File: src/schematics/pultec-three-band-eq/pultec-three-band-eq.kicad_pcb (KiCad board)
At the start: 2 copper layers, 55 parts, among them J1 IN, J10 Low Boost Select Return, J11 Low Boost Level, J12 Hi Cut Select Return, J13 Frequency Selector Send, J19 Inductor Return, J2 OUT, J20 Boost High Q, J21 Boost High, J22 100mH, J23 200mH, J24 300mH, J25 600mH, J3 Hi Cut Select Send, J4 HI CUT, J5 Low Cut Select Send, J6 Low Boost Select Send, J7 Low Cut Level, J8 High Boost Selector Return, J9 Low Cut Select Return

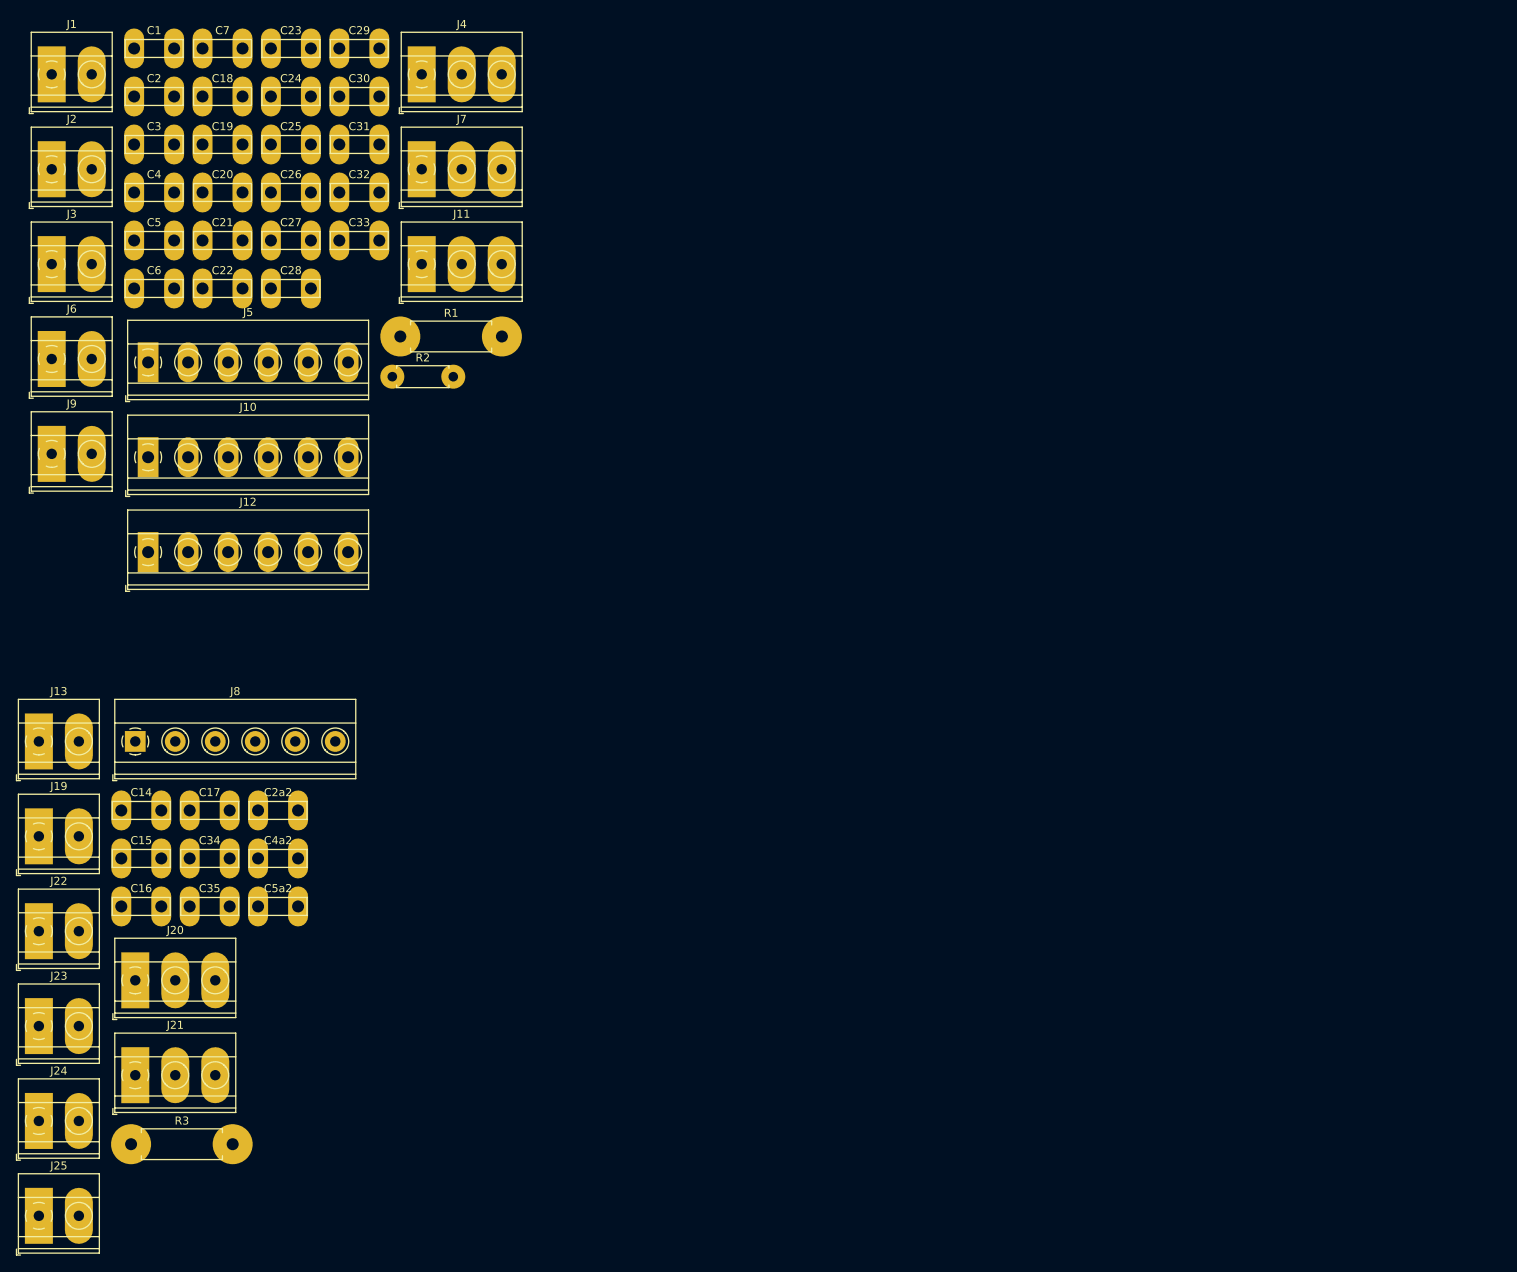
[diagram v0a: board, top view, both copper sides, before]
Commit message: - fixed unrouted traces
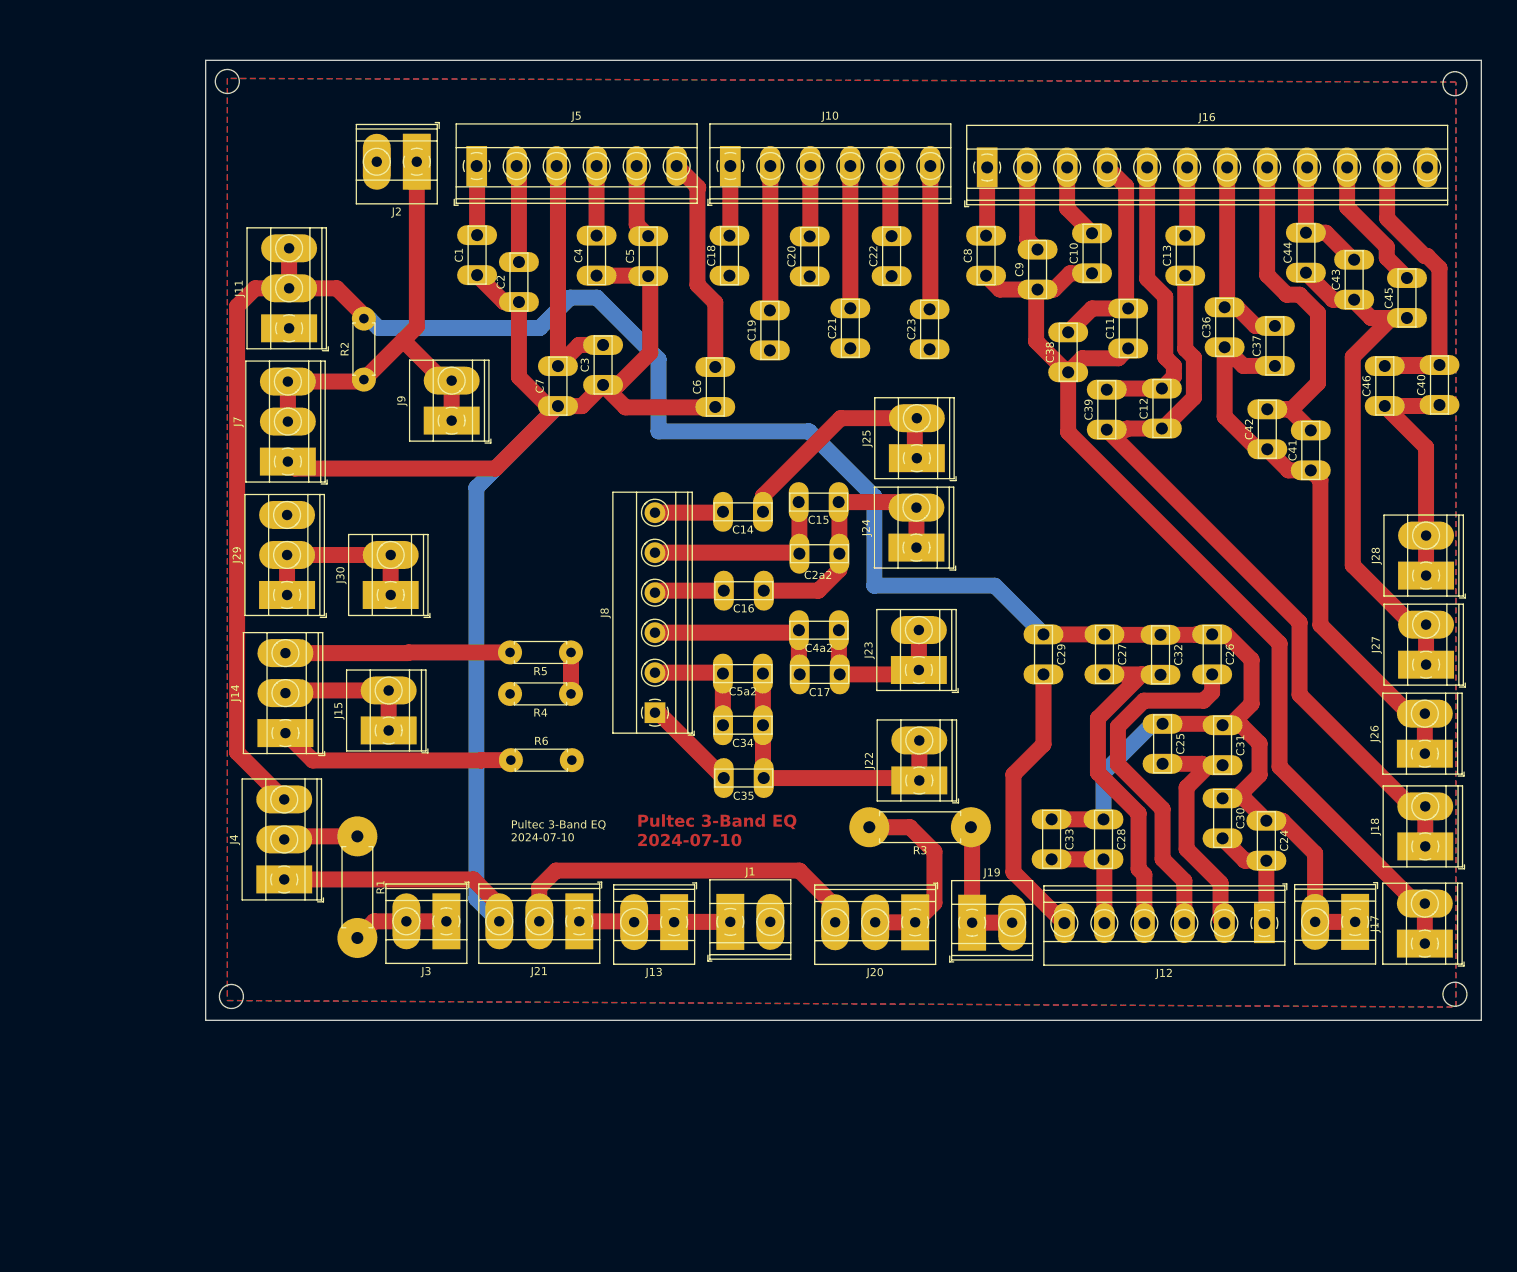
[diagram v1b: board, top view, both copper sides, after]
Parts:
- added C10: 47n, OL Library:C_Rect_L7.0mm_W2.0mm_P5.00mm_Fat_Pad, F.Cu at (151.2, 47.3)
- added C11: 22n, OL Library:C_Rect_L7.0mm_W2.0mm_P5.00mm_Fat_Pad, F.Cu at (155.8, 56.7)
- added C12: 22n, OL Library:C_Rect_L7.0mm_W2.0mm_P5.00mm_Fat_Pad, F.Cu at (160.0, 66.8)
- added C13: 12n, OL Library:C_Rect_L7.0mm_W2.0mm_P5.00mm_Fat_Pad, F.Cu at (162.9, 47.6)
- added C36: 12n, OL Library:C_Rect_L7.0mm_W2.0mm_P5.00mm_Fat_Pad, F.Cu at (167.8, 56.6)
- added C37: 2n2, OL Library:C_Rect_L7.0mm_W2.0mm_P5.00mm_Fat_Pad, F.Cu at (174.1, 58.9)
- added C38: 3n3, OL Library:C_Rect_L7.0mm_W2.0mm_P5.00mm_Fat_Pad, F.Cu at (148.3, 59.7)
- added C39: 3n3, OL Library:C_Rect_L7.0mm_W2.0mm_P5.00mm_Fat_Pad, F.Cu at (153.1, 66.9)
- added C40: 1n, OL Library:C_Rect_L7.0mm_W2.0mm_P5.00mm_Fat_Pad, F.Cu at (194.7, 63.8)
- added C41: 4n7, OL Library:C_Rect_L7.0mm_W2.0mm_P5.00mm_Fat_Pad, F.Cu at (178.6, 72.0)
- added C42: 1n5, OL Library:C_Rect_L7.0mm_W2.0mm_P5.00mm_Fat_Pad, F.Cu at (173.1, 69.3)
- added C43: 4n7, OL Library:C_Rect_L7.0mm_W2.0mm_P5.00mm_Fat_Pad, F.Cu at (184.0, 50.6)
- added C44: 2n2, OL Library:C_Rect_L7.0mm_W2.0mm_P5.00mm_Fat_Pad, F.Cu at (178.0, 47.3)
- added C45: 4n7, OL Library:C_Rect_L7.0mm_W2.0mm_P5.00mm_Fat_Pad, F.Cu at (190.6, 52.9)
- added C46: 2n2, OL Library:C_Rect_L7.0mm_W2.0mm_P5.00mm_Fat_Pad, F.Cu at (187.8, 63.9)
- added C8: 33n, OL Library:C_Rect_L7.0mm_W2.0mm_P5.00mm_Fat_Pad, F.Cu at (138.0, 47.7)
- added C9: 150n, OL Library:C_Rect_L7.0mm_W2.0mm_P5.00mm_Fat_Pad, F.Cu at (144.4, 49.4)
- added J14: Mid bst/cut switch, OL Library:TerminalBlock_Phoenix_MKDS-1,5-3_1x03_P5.00mm_Horizontal Fat Pad, F.Cu at (50.4, 104.8)
- added J15: Mid Sel Ret, OL Library:TerminalBlock_Phoenix_MKDS-1,5-2_1x02_P5.00mm_Horizontal Fat Pad, F.Cu at (63.3, 104.5)
- added J16: Mid Sel Ret, OL Library:TerminalBlock_Phoenix_MKDS-1,5-12_1x12_P5.00mm_Horizontal_Fat_Pad, F.Cu at (138.1, 34.1)
- added J17: 2H, OL Library:TerminalBlock_Phoenix_MKDS-1,5-2_1x02_P5.00mm_Horizontal Fat Pad, F.Cu at (192.8, 131.1)
- added J18: 1H, OL Library:TerminalBlock_Phoenix_MKDS-1,5-2_1x02_P5.00mm_Horizontal Fat Pad, F.Cu at (192.9, 119.0)
- added J26: .45H, OL Library:TerminalBlock_Phoenix_MKDS-1,5-2_1x02_P5.00mm_Horizontal Fat Pad, F.Cu at (192.8, 107.4)
- added J27: .22H, OL Library:TerminalBlock_Phoenix_MKDS-1,5-2_1x02_P5.00mm_Horizontal Fat Pad, F.Cu at (193.0, 96.3)
- added J28: .1H, OL Library:TerminalBlock_Phoenix_MKDS-1,5-2_1x02_P5.00mm_Horizontal Fat Pad, F.Cu at (193.0, 85.1)
- added J29: Mid Lvl (47 Log), OL Library:TerminalBlock_Phoenix_MKDS-1,5-3_1x03_P5.00mm_Horizontal Fat Pad, F.Cu at (50.6, 87.6)
- added J30: Mid Sel Snd, OL Library:TerminalBlock_Phoenix_MKDS-1,5-2_1x02_P5.00mm_Horizontal Fat Pad, F.Cu at (63.6, 87.6)
- added R4: 100K, OL Library:R_Axial_DIN0207_L6.3mm_D2.5mm_P7.62mm_Horizontal, F.Cu at (86.1, 99.9)
- added R5: 4K7, OL Library:R_Axial_DIN0207_L6.3mm_D2.5mm_P7.62mm_Horizontal, F.Cu at (86.1, 94.7)
- added R6: 1K, OL Library:R_Axial_DIN0207_L6.3mm_D2.5mm_P7.62mm_Horizontal, F.Cu at (78.6, 108.2)
- J10: value Low Boost Select Return -> Lo Boost Sel Ret
- J11: value Low Boost Level -> Lo Boost Lvl
- J12: value Hi Cut Select Return -> Hi Cut Sel Ret
- J13: value Frequency Selector Send -> Hi Boost Sel Snd
- J19: value Inductor Return -> Hi Boost Sel Ret
- J20: value Boost High Q -> Hi Boost Q
- J21: value Boost High -> Hi Boost Lvl
- J3: value Hi Cut Select Send -> Hi Cut Sel Snd
- J4: value HI CUT -> Hi Cut Lvl
- J5: value Low Cut Select Send -> Lo Cut Sel Snd
- J6: value Low Boost Select Send -> Lo Boost Sel Snd
- J7: value Low Cut Level -> Low Cut Lvl
- J8: value High Boost Selector Return -> Hi Boost Sel Rtn
- J9: value Low Cut Select Return -> Low Cut Sel Ret
- moved J6 177.5 mm to (184.1, 128.4), turned to 180 degrees
- moved C24 153.9 mm to (173.0, 115.8), turned to -90 degrees
- moved J12 147.0 mm to (172.8, 128.6), turned to 180 degrees
- moved J25 145.0 mm to (129.3, 70.5), turned to 90 degrees
- moved C30 141.0 mm to (167.6, 113.0), turned to -90 degrees
- moved J1 135.7 mm to (106.0, 128.4)
- moved C25 132.9 mm to (160.1, 103.7), turned to -90 degrees
- moved C31 132.1 mm to (167.6, 103.8), turned to -90 degrees
- moved J24 131.0 mm to (129.3, 81.6), turned to 90 degrees
- moved C26 130.0 mm to (166.2, 92.5), turned to -90 degrees
- moved C28 123.4 mm to (152.7, 115.6), turned to -90 degrees
- moved J23 118.7 mm to (129.6, 96.9), turned to 90 degrees
- moved J19 117.2 mm to (136.2, 128.5)
- moved C32 116.6 mm to (159.8, 92.5), turned to -90 degrees
- moved C27 115.2 mm to (152.8, 92.5), turned to -90 degrees
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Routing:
- net /LO BOOST IN: track 0.00 -> 315.2 mm
- net /HI BOOST OUT: track 0.00 -> 205.5 mm
- net Net-(J17-Pin_1): track 0.00 -> 126.4 mm
- net Net-(J18-Pin_1): track 0.00 -> 97.9 mm
- net Net-(J26-Pin_1): track 0.00 -> 71.9 mm
- net Net-(J27-Pin_1): track 0.00 -> 67.2 mm
- net /OUT: track 0.00 -> 57.7 mm
- net Net-(J20-Pin_3): track 0.00 -> 46.0 mm
- net Net-(J12-Pin_4): track 0.00 -> 45.1 mm
- net Net-(J16-Pin_8): track 0.00 -> 44.7 mm
- net Net-(J12-Pin_3): track 0.00 -> 43.8 mm
- net Net-(J16-Pin_11): track 0.00 -> 41.4 mm
- net Net-(J22-Pin_1): track 0.00 -> 37.7 mm
- net Net-(J16-Pin_5): track 0.00 -> 36.6 mm
- net Net-(J12-Pin_6): track 0.00 -> 35.3 mm
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- added copper zone on B.Cu, net GND
- added copper zone on F.Cu, net GND
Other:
- board outline added: 159.5 x 120 mm
- board text added: "Pultec 3-Band EQ 2024-07-10"

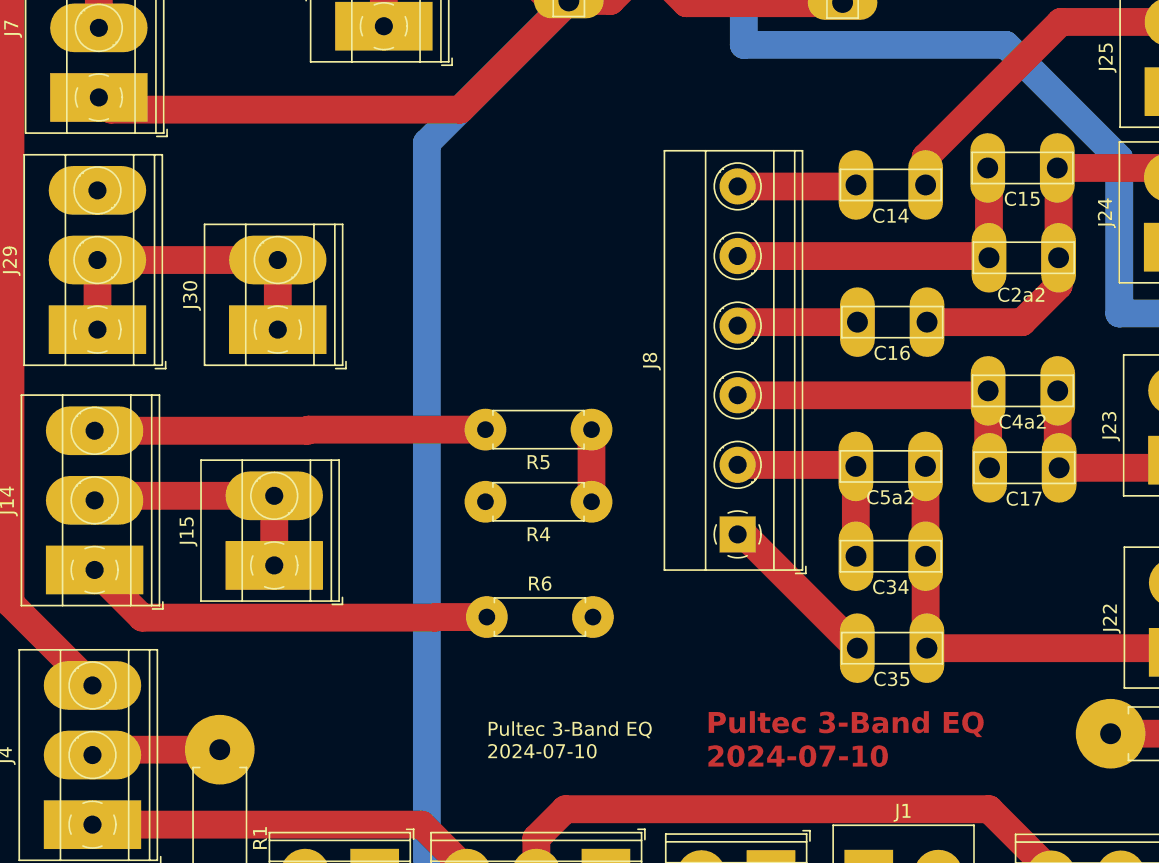
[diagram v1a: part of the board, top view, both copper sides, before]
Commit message: - fixed issue with hierarchical label - fixed unrouted trace related to issue with hierarchical label - Updated PCB identifier in front copper and front fab layers to use variables instead of hard-coded dates and revisions.
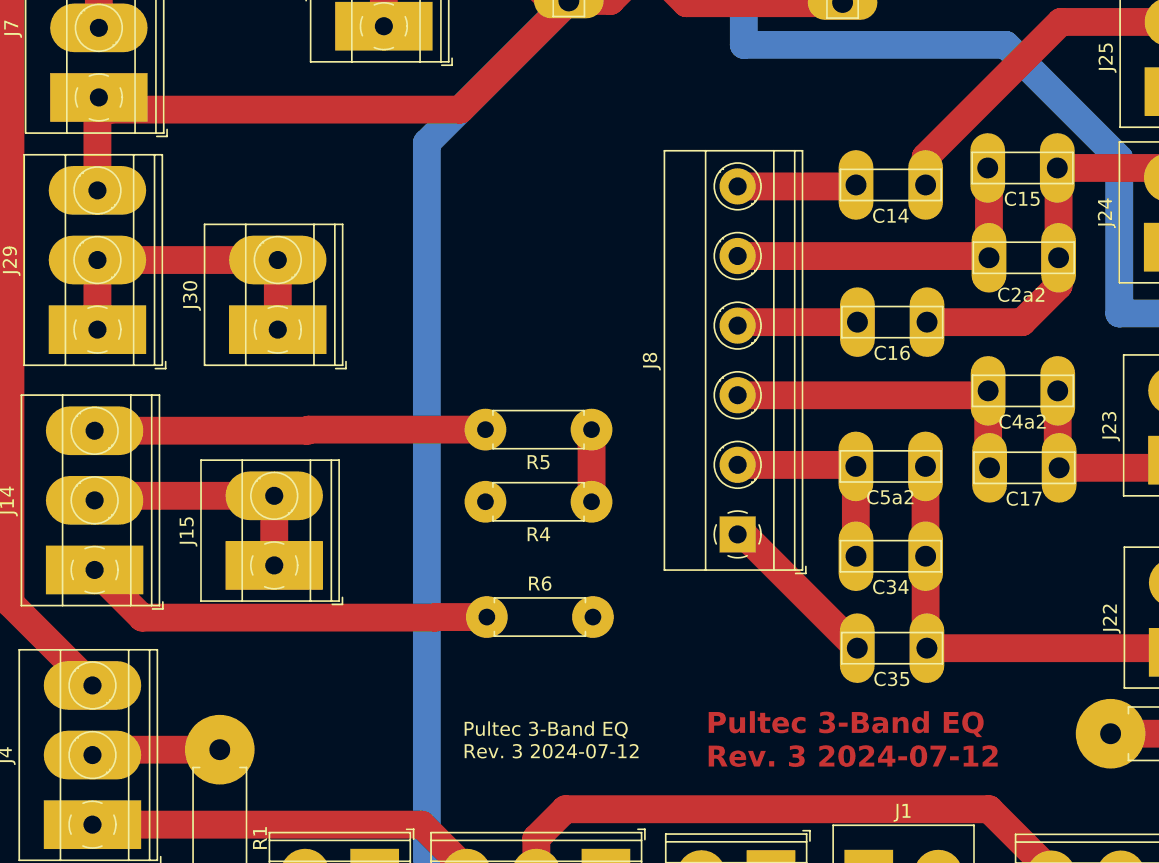
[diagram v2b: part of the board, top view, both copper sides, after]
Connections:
- J29 pad 3: /pultec-mid-band/HI BOOST OUT -> /HI BOOST OUT
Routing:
- net /HI BOOST OUT: track 205.5 -> 212.2 mm
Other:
- board text added: "${TITLE} Rev. ${REVISION} ${ISSUE_DATE}"
- board text removed: "Pultec 3-Band EQ 2024-07-10"
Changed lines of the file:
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@@
 	(title_block
 		(title "Pultec 3-Band EQ")
-		(date "2024-07-10")
-		(rev "2")
+		(date "2024-07-12")
+		(rev "3")
 	)
 	(layers
@@
 	(net 57 "Net-(J14-Pin_2)")
 	(net 58 "Net-(J29-Pin_1)")
-	(net 59 "/pultec-mid-band/HI BOOST OUT")
-	(net 60 "/pultec-mid-band/IN")
+	(net 59 "/pultec-mid-band/IN")
 	(footprint "OL Library:C_Rect_L7.0mm_W2.0mm_P5.00mm_Fat_Pad"
 		(layer "F.Cu")
@@
 			(layers "*.Cu" "*.Mask")
 			(remove_unused_layers no)
-			(net 60 "/pultec-mid-band/IN")
+			(net 59 "/pultec-mid-band/IN")
 			(pintype "passive")
 		)
@@
 			(layers "*.Cu" "*.Mask")
 			(remove_unused_layers no)
-			(net 59 "/pultec-mid-band/HI BOOST OUT")
+			(net 2 "/HI BOOST OUT")
 			(pinfunction "Pin_3")
 			(pintype "passive")
@@
 			(layers "*.Cu" "*.Mask")
 			(remove_unused_layers no)
-			(net 60 "/pultec-mid-band/IN")
+			(net 59 "/pultec-mid-band/IN")
 			(pintype "passive")
 		)
@@
 		(layer "Edge.Cuts")
 	)
-	(gr_text "Pultec 3-Band EQ\n2024-07-10"
+	(gr_text "${TITLE}\nRev. ${REVISION} ${ISSUE_DATE}"
 		(at 94.3356 119.126 0)
 		(layer "F.Cu")
@@
 		)
 	)
-	(gr_text "Pultec 3-Band EQ\n2024-07-10"
-		(at 78.5876 118.4656 0)
+	(gr_text "${TITLE}\nRev. ${REVISION} ${ISSUE_DATE}"
+		(at 76.8604 118.4656 0)
 		(layer "F.SilkS")
 		(effects
@@
 	)
 	(segment
+		(start 50.614206 70.9816)
+		(end 50.715806 70.88)
+		(width 2)
+		(layer "F.Cu")
+		(net 2)
+	)
+	(segment
+		(start 50.614206 77.5576)
+		(end 50.614206 70.9816)
+		(width 2)
+		(layer "F.Cu")
+		(net 2)
+	)
+	(segment
 		(start 74.367006 47.5778)
 		(end 77.730606 50.9414)
@@
 		(width 2)
 		(layer "F.Cu")
-		(net 60)
+		(net 59)
 	)
 	(zone
